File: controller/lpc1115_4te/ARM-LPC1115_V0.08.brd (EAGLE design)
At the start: 66 x 57.9 mm, 52 parts, among them IC2 MC34063AP, IC3 MCP1702-33, Q1 BC557B, Q3 BC640C, T1 BC547C

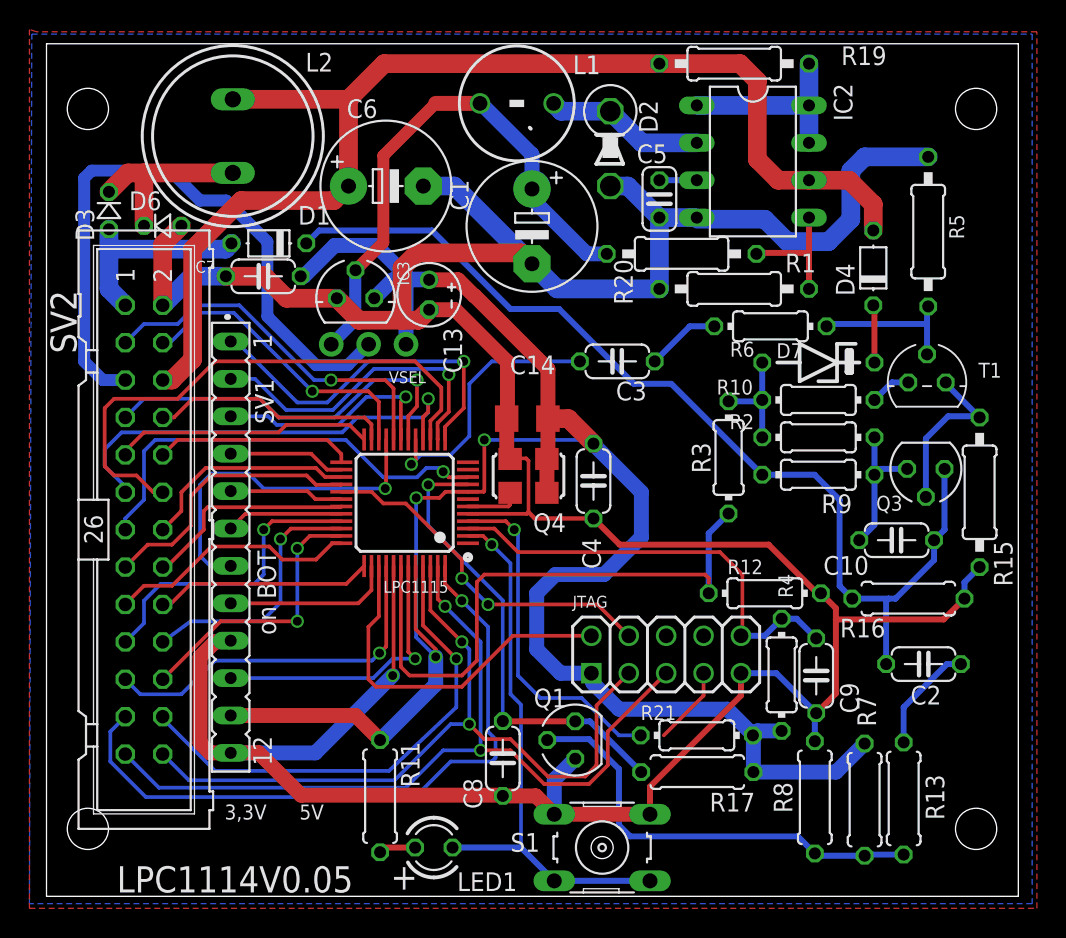
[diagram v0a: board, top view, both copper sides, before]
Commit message: Improve layout
Changed routing to create better ground plane on bottom layer.
Add C11 to proviode better/more stable voltage supply to the CPU.
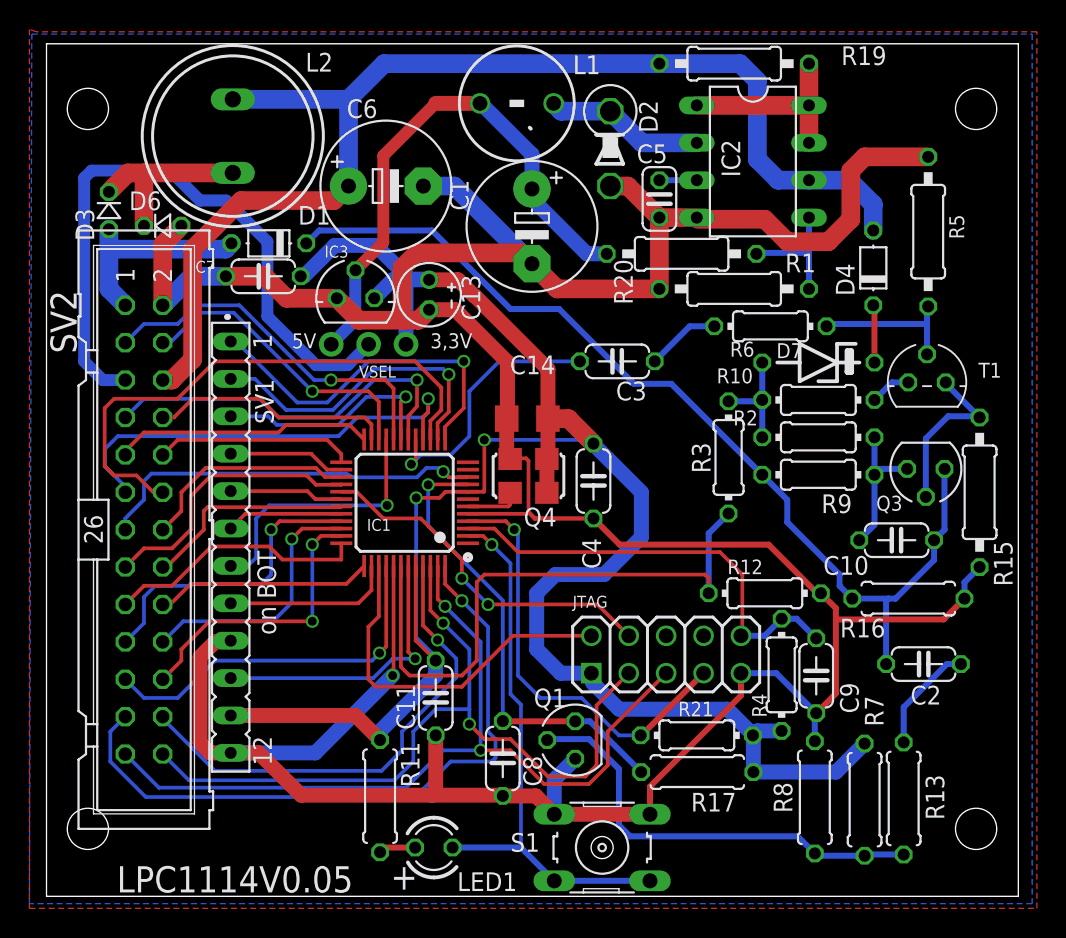
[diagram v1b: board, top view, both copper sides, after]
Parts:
- added C11: 100n, rcl:C050-024X044
- IC1: value (none) -> LPC1115
- JTAG: value (none) -> J
- Q4: value (none) -> 12MHz
- SV1: value (none) -> LT
- SV2: value (none) -> A
- VSEL: value (none) -> V
- renumbered LPC1115 to IC1
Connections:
- net BUS_VOLTAGE renamed BUS_V
- removed net ISP_ENABLE: JTAG.7
- net GND: now also C11.1
- net ISP_EN: now also JTAG.7
- net VCC_3V3: now also C11.2
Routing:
- net ISP_EN: track 23.4 -> 29.4 mm
- net LT7: track 23.9 -> 18.4 mm
- net ISP_ENABLE: track 5.34 -> 0.00 mm
- net GND: track 242.7 -> 246.9 mm
- net IO5: track 29.8 -> 26.6 mm
- net DRAIN: track 68.9 -> 66.8 mm
- net IO16: track 52.6 -> 54.2 mm
- net TXD: track 17.1 -> 17.8 mm
- net IO12: track 19.1 -> 19.7 mm
- net VCC_3V3: track 144.9 -> 145.2 mm, vias 3 -> 2

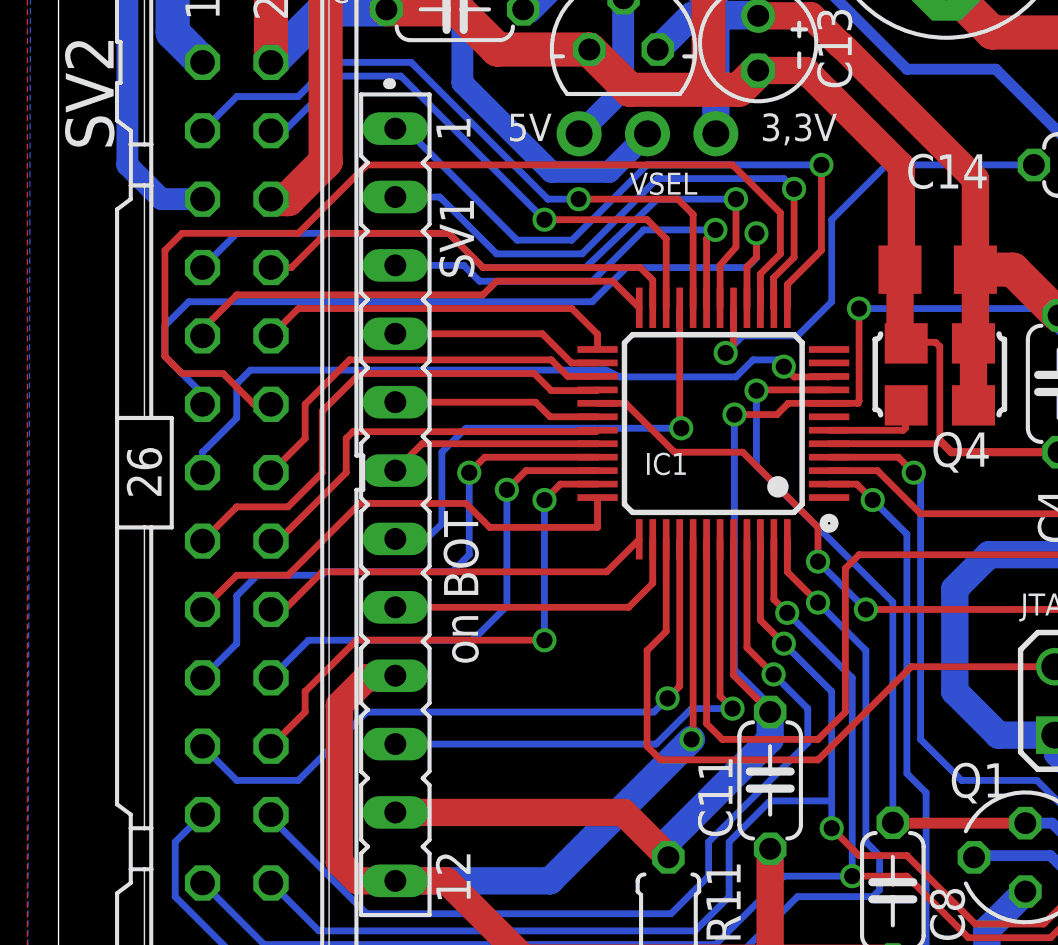
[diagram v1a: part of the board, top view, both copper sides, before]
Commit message: Exchange PWM and LT9
To support a LPC11Uxx device and have the two pins required for the USB on
the LED/Taster pinhead the old PWM and LT9 have been swaped.
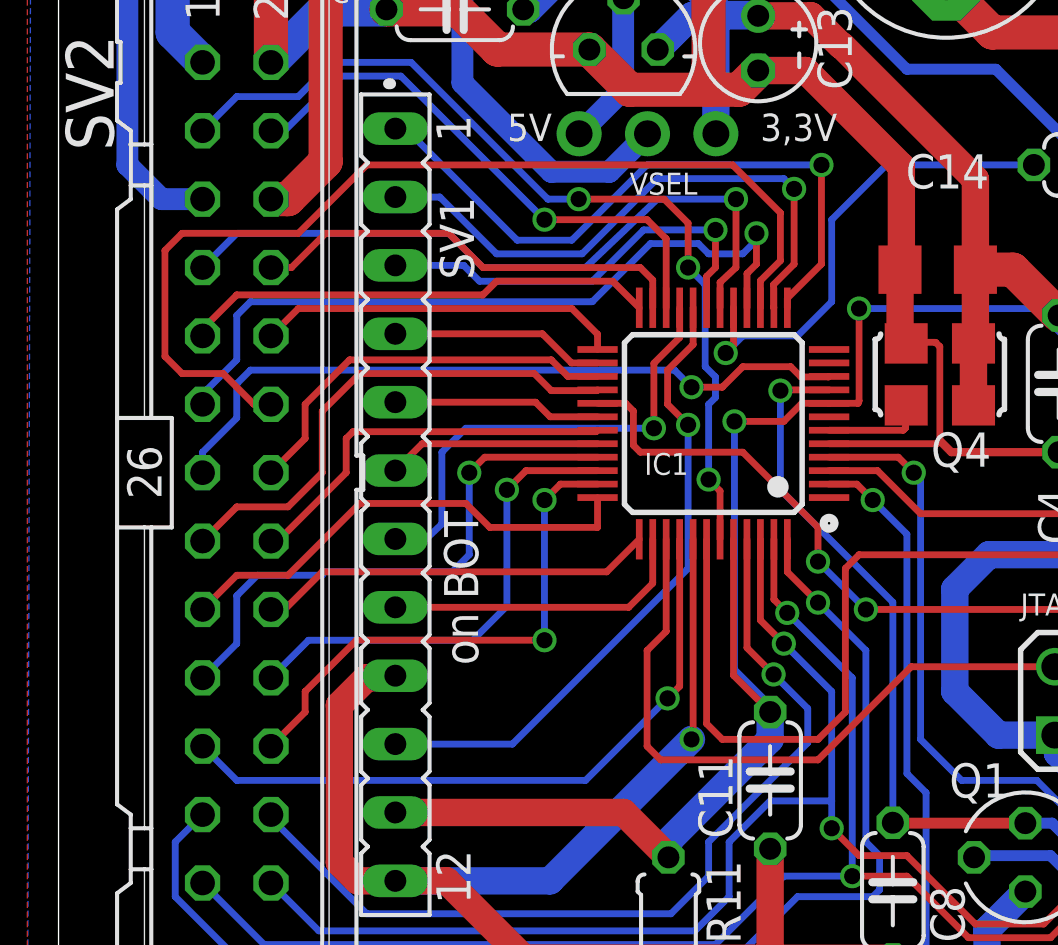
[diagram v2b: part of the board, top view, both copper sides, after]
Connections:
- net LT9: now also IC1.20; no longer IC1.43
- net PWM: now also IC1.43; no longer IC1.20
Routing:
- net PWM: track 25.1 -> 34.0 mm, vias 1 -> 3
- net LT9: track 19.6 -> 24.0 mm
- net SDA: track 30.3 -> 27.8 mm
- net EIB_IN: track 31.7 -> 30.4 mm
- net SWCLK: track 24.3 -> 25.1 mm
- net LT7: track 18.4 -> 17.8 mm

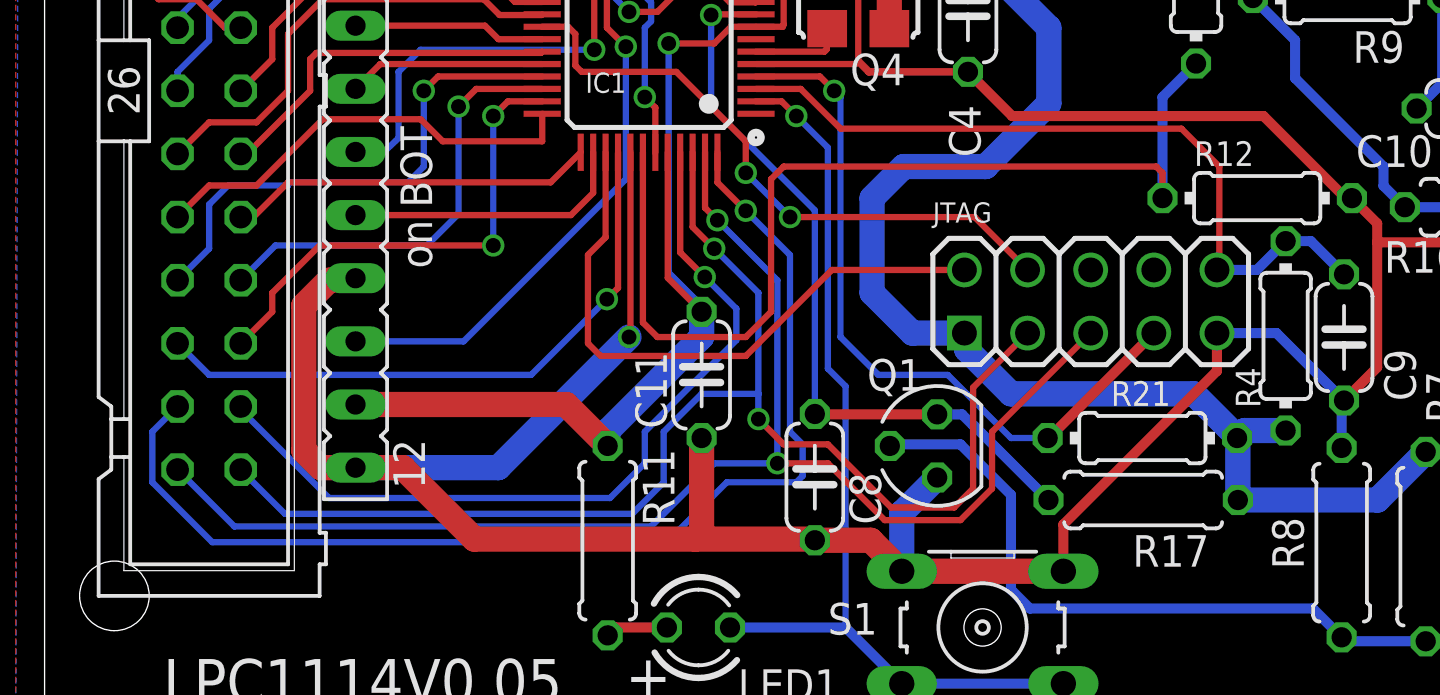
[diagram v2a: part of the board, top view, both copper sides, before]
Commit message: Additional GND added to App pinheader
On pin 21 a new GND has been added. The following pins have been rearraged
to keep all ADV channels.
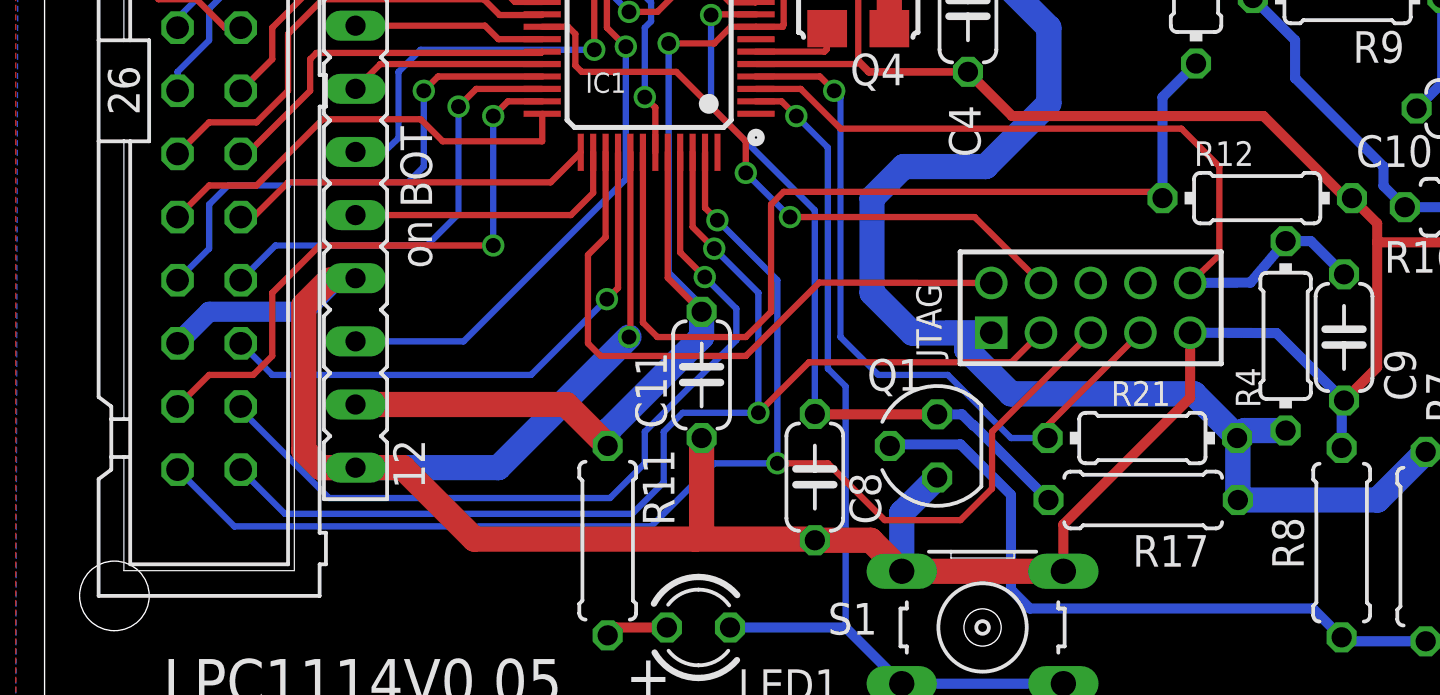
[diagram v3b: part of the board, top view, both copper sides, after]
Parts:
- JTAG: device microbuilder:2X05 -> pinhead-2:2X05M
- moved JTAG 0.25 mm to (43.1, 16.7)
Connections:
- removed net IO16: IC1.46, JTAG.3, SV2.26
- net GND: now also SV2.21
- net IO11: now also SV2.22; no longer SV2.21
- net IO12: now also SV2.23; no longer SV2.22
- net IO13: now also IC1.45, SV2.24; no longer IC1.48, SV2.23
- net IO14: now also IC1.47, JTAG.5, SV2.25; no longer IC1.45, SV2.24
- net IO15: now also IC1.46, JTAG.3, SV2.26; no longer IC1.47, JTAG.5, SV2.25
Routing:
- net IO16: track 54.2 -> 0.00 mm, vias 2 -> 0
- net IO14: track 33.4 -> 57.9 mm, vias 1 -> 2
- net IO13: track 46.2 -> 33.4 mm
- net IO15: track 57.9 -> 48.7 mm
- net GND: track 246.9 -> 255.8 mm
- net IO12: track 19.7 -> 24.3 mm
- net IO11: track 25.2 -> 22.6 mm
- net RESET: track 30.3 -> 32.6 mm
- net BUS_V: track 41.1 -> 39.0 mm
- net VCC_3V3: track 145.2 -> 147.1 mm
- net SWDIO: track 24.8 -> 25.6 mm
- net SWCLK: track 25.1 -> 25.8 mm

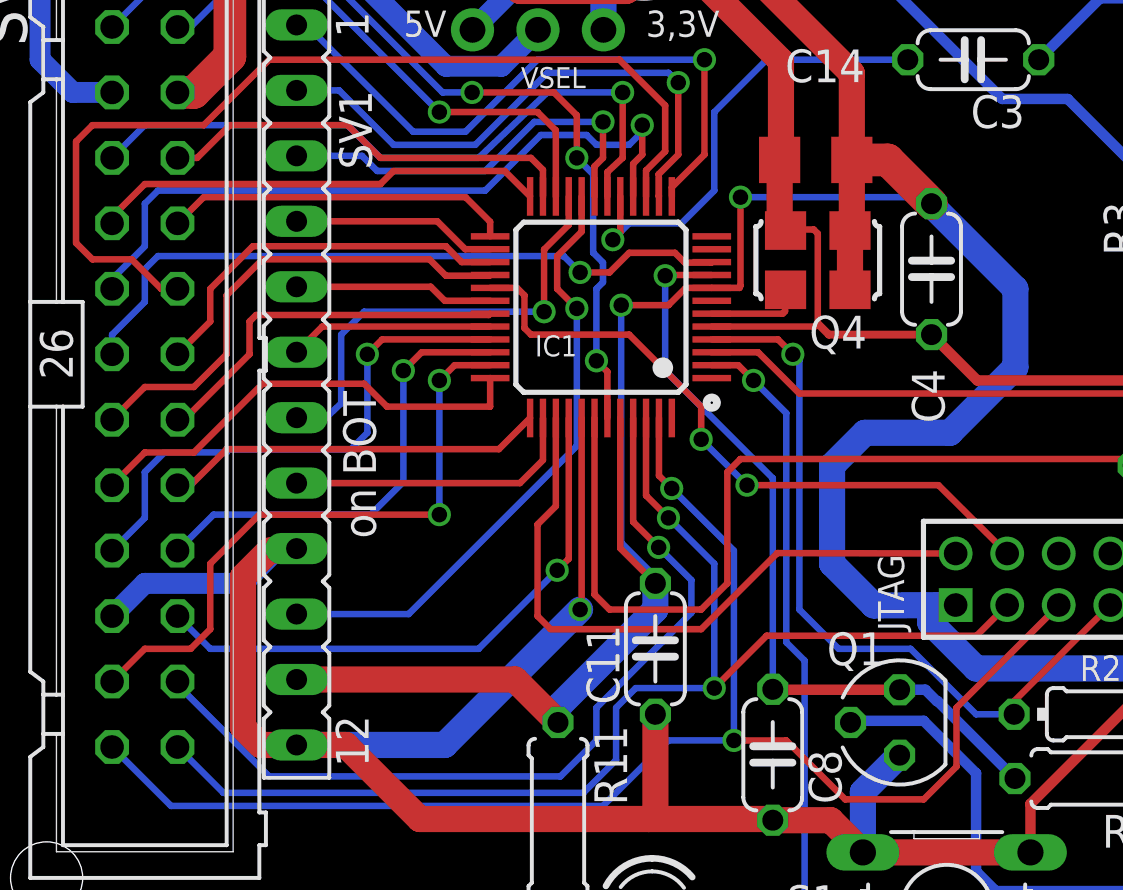
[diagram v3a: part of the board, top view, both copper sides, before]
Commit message: Improoved GND plane on BOT
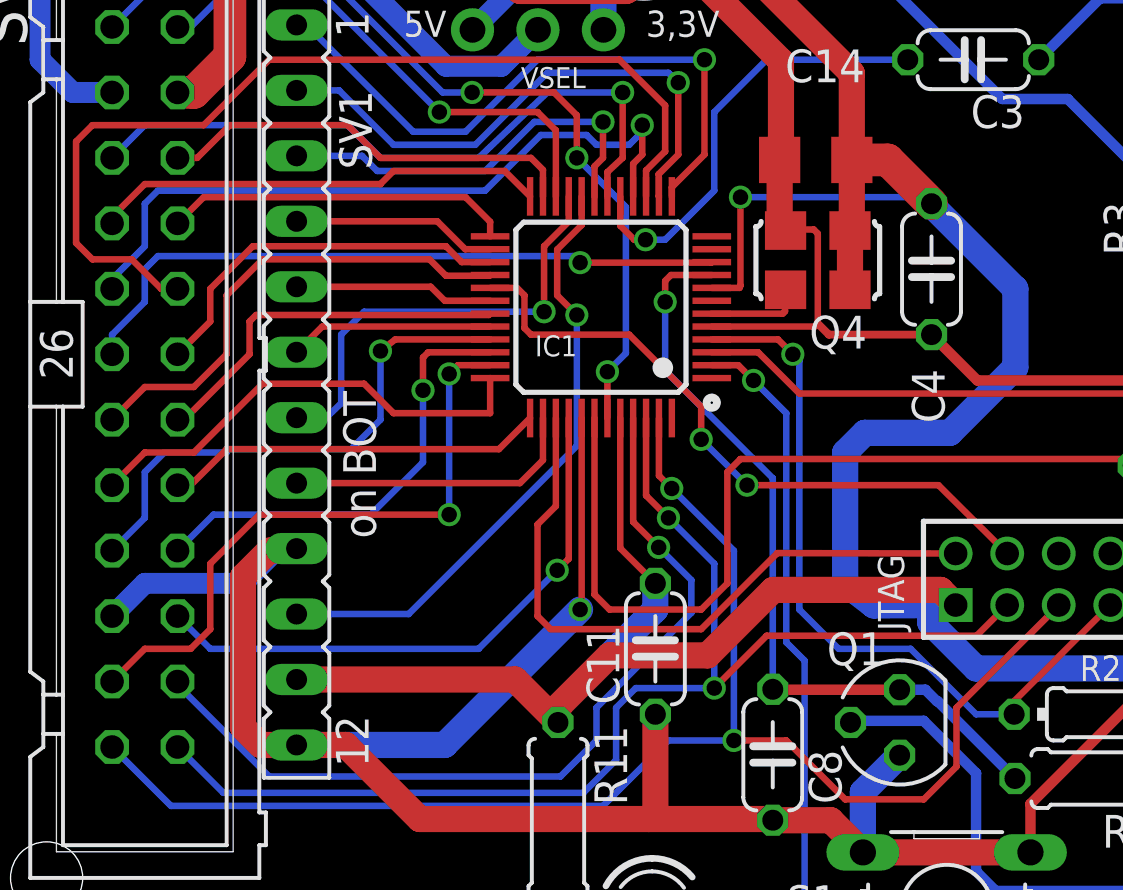
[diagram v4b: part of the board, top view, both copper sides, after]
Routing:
- net VCC_3V3: track 147.1 -> 149.6 mm, vias 2 -> 1
- net EIB_OUT: track 17.9 -> 17.2 mm
- net IO5: track 26.8 -> 26.2 mm
